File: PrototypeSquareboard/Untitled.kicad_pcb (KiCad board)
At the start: 2 copper layers, 131.9 x 97.8 mm, 35 parts

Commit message: square and flower boards at V4
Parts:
- added G***: LOGO, Symbol:UCR_logo_1.4cm, F.Cu at (71.8, 87.0)
- added G***: LOGO, Symbol:Consortium_logo_1pt4cm, F.Cu at (71.6, 99.0)
- G*** (x2): moved to B.Cu
- REF** (x4): footprint SiPM:S14160-3015PS_copy -> SiPM:S14160-3015PS_copy2
- moved G*** 70.4 mm to (89.0, 40.0), turned to 180 degrees
- moved G*** 35.8 mm to (86.6, 74.4), turned to 180 degrees
- moved G*** 8.11 mm to (138.7, 82.2)
- moved REF** 2.20 mm to (66.0, 36.6)
- moved REF** 2.10 mm to (66.0, 47.7)
- moved REF** 1.20 mm to (66.0, 59.2)
- moved REF** 1.00 mm to (66.0, 70.6)
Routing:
- net (no net): track 2555.4 -> 2562.2 mm
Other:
- board text added: "1 2 3 4"
- board text added: "Designed by Sebouh J Paul Version 4"
- board text removed: "1"
- board text removed: "2"
- board text removed: "3"
- board text removed: "4"
- board text removed: "Designed by Sebouh J Paul Version 3"

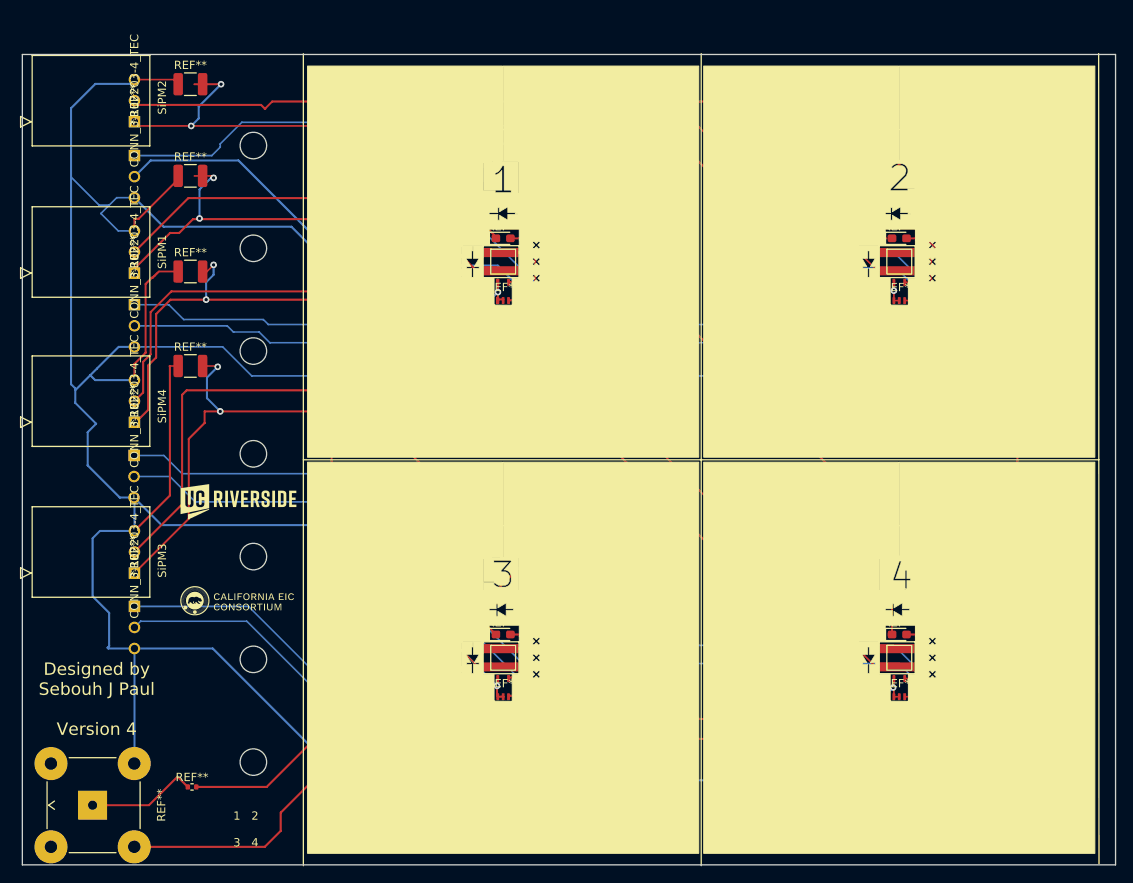
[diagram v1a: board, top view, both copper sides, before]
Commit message: v5 of the prototype hexboard and squareboards:  added label to capacitors and resistors; moved temperature sensors to periphery; added 0.1 mm back to top and bottom of boards
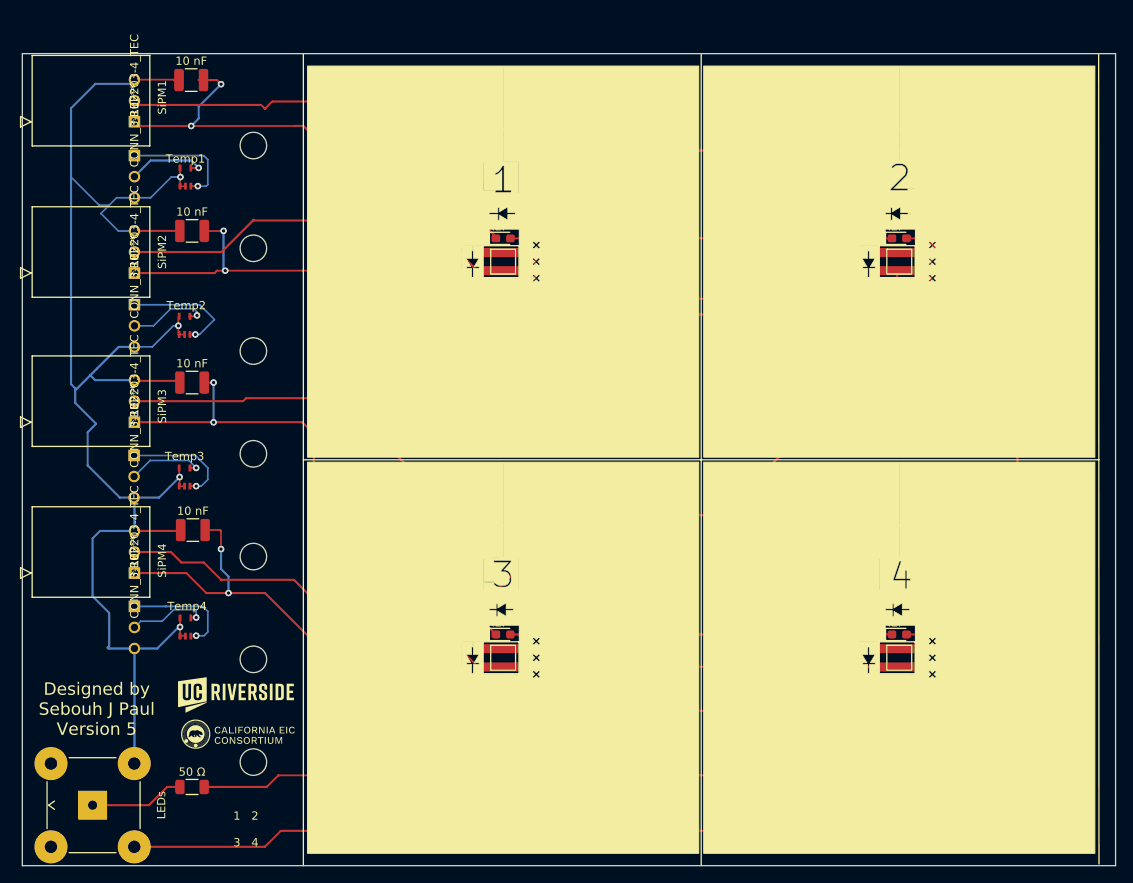
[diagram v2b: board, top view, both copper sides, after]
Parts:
- removed ? (x2): , 
- 10 nF: renamed from REF** (x4)
- 50 Ω: renamed from REF**; value R_0402_1005Metric -> R_1206_3216Metric; footprint Resistor_SMD:R_0402_1005Metric -> Resistor_SMD:R_1206_3216Metric
- moved Temp4 86.4 mm to (65.4, 102.1)
- moved Temp2 86.3 mm to (65.3, 65.7)
- moved Temp3 46.1 mm to (65.3, 84.0)
- moved Temp1 40.7 mm to (65.4, 47.8)
- moved G*** 23.3 mm to (71.5, 110.3)
- moved 10 nF 19.8 mm to (66.3, 90.4)
- moved G*** 16.1 mm to (71.7, 115.1)
- moved 10 nF 13.4 mm to (66.2, 72.6)
- moved 10 nF 6.64 mm to (66.2, 54.3)
- moved G*** 6.61 mm to (90.9, 79.4)
- moved G*** 1.08 mm to (90.0, 39.6)
- moved 10 nF 0.51 mm to (66.1, 36.1)
- renumbered REF** to LEDs, REF** to Temp1, REF** to Temp2, REF** to Temp3, REF** to Temp4
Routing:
- net (no net): track 2562.2 -> 1613.3 mm
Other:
- board size 131.9 x 97.8 mm -> 131.9 x 98 mm
- board text added: "Designed by Sebouh J Paul Version 5"
- board text removed: "Designed by Sebouh J Paul Version 4"

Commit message: v6 of square and hex boards: traces in back in the area where the scints are to be placed.
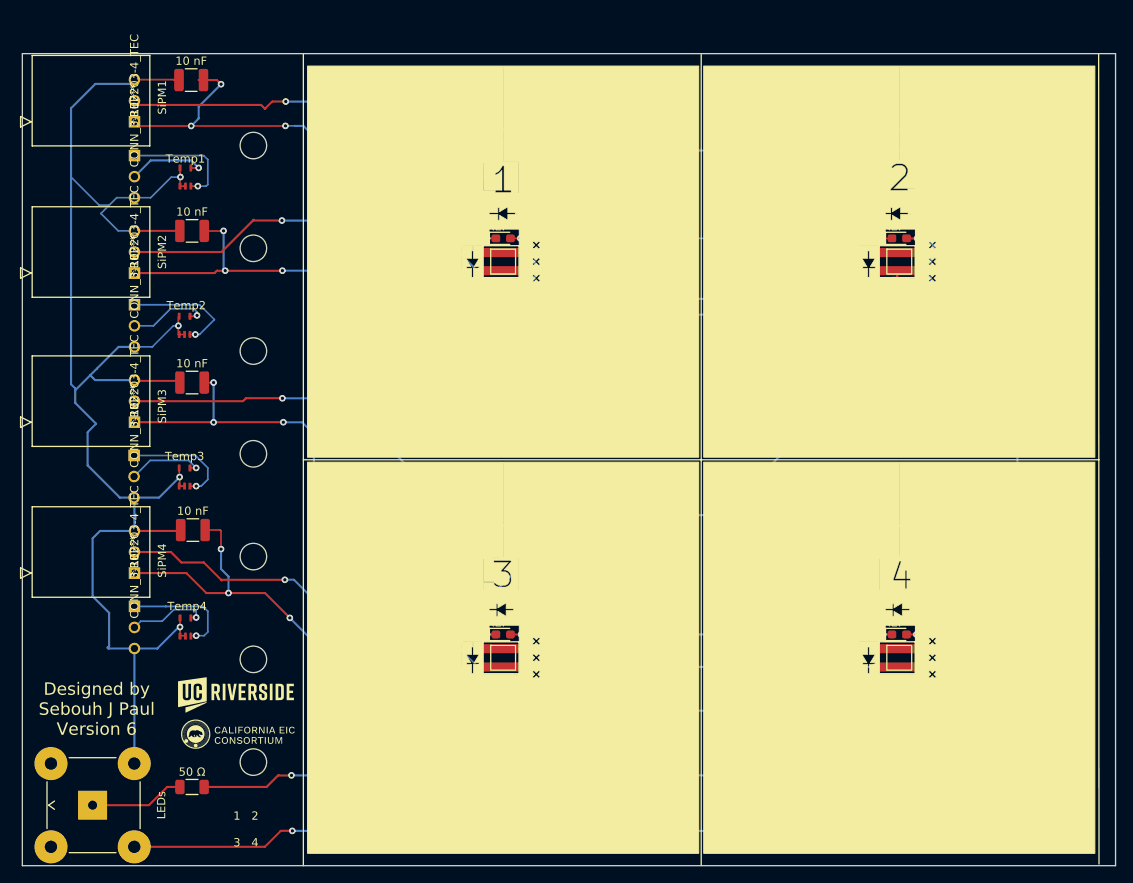
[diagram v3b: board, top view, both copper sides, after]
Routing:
- net (no net): track 1613.3 -> 1612.2 mm, vias 20 -> 46
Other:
- board text added: "Designed by Sebouh J Paul Version 6"
- board text removed: "Designed by Sebouh J Paul Version 5"

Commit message: removed extraneous traces on front of square-cell board
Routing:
- net (no net): track 1612.2 -> 1604.7 mm
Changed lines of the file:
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@@
   (segment (start 63.9725 36.0475) (end 64.525 36.6) (width 0.2) (layer "F.Cu") (net 0))
   (segment (start 54.2 123.6) (end 61 123.6) (width 0.25) (layer "F.Cu") (net 0))
-  (segment (start 106.2 64.4) (end 107 64.4) (width 0.25) (layer "F.Cu") (net 0))
   (segment (start 64.7 85.05) (end 64.65 85.1) (width 0.2) (layer "F.Cu") (net 0))
   (segment (start 69.7 92.7) (end 69.7 90.5) (width 0.2) (layer "F.Cu") (net 0))
@@
   (segment (start 64.55 66.8) (end 65.2 66.8) (width 0.2) (layer "F.Cu") (net 0))
   (segment (start 63.525 90.5075) (end 64.7175 90.5075) (width 0.25) (layer "F.Cu") (net 0))
-  (segment (start 94.45 52.95) (end 96.9 55.4) (width 0.25) (layer "F.Cu") (net 0))
   (segment (start 59.2501 56.8475) (end 69.7525 56.8475) (width 0.25) (layer "F.Cu") (net 0))
   (segment (start 67.613497 94.313497) (end 69.7 96.4) (width 0.25) (layer "F.Cu") (net 0))
@@
   (segment (start 104.615 55.2) (end 105.8 55.2) (width 0.2) (layer "F.Cu") (net 0))
   (segment (start 59.2501 93.0475) (end 63.6475 93.0475) (width 0.25) (layer "F.Cu") (net 0))
-  (segment (start 132.3 86.3) (end 130 88.6) (width 0.25) (layer "F.Cu") (net 0))
   (segment (start 102.865 55.2) (end 101.8 55.2) (width 0.2) (layer "F.Cu") (net 0))
   (segment (start 152.215 55.2) (end 153.7 55.2) (width 0.25) (layer "F.Cu") (net 0))

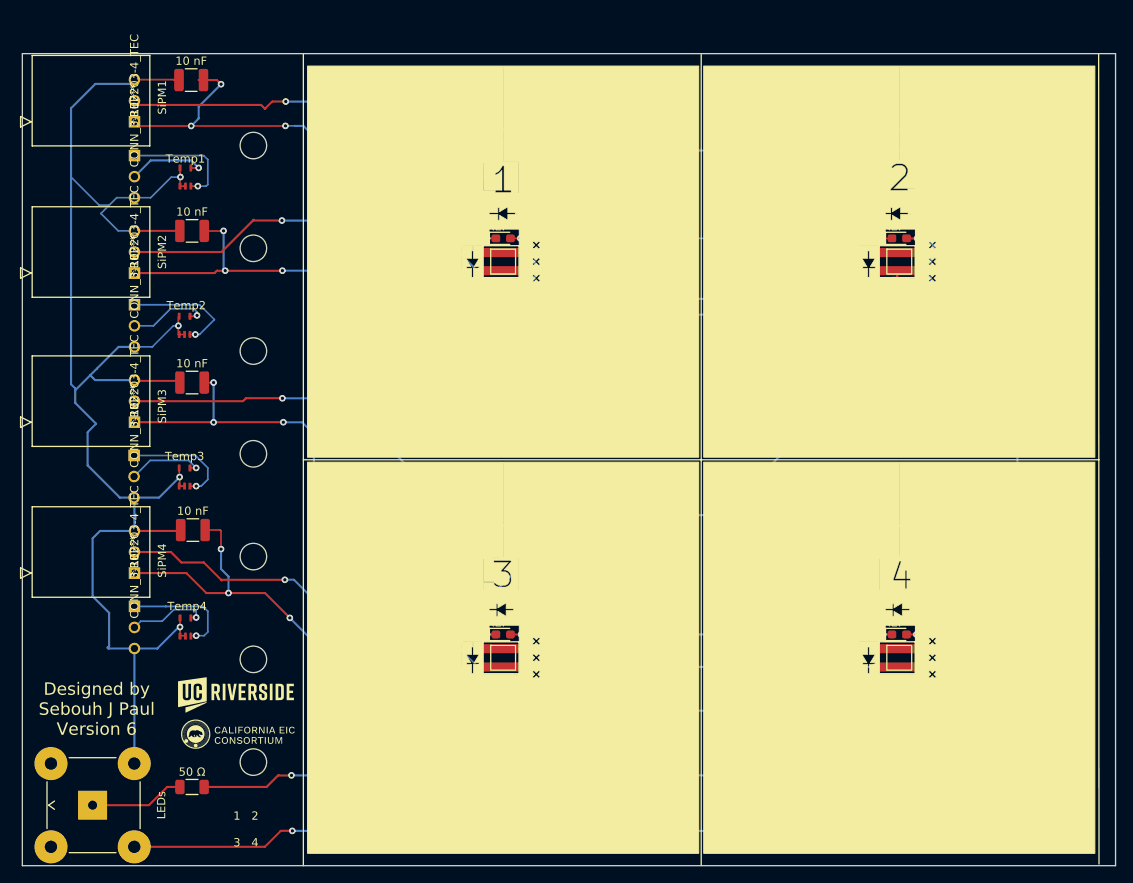
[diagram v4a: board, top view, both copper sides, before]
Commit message: v7 square board.  1.3 mm SiPMs, vias inside dimples, and excessive silkscreen removed outside dimple
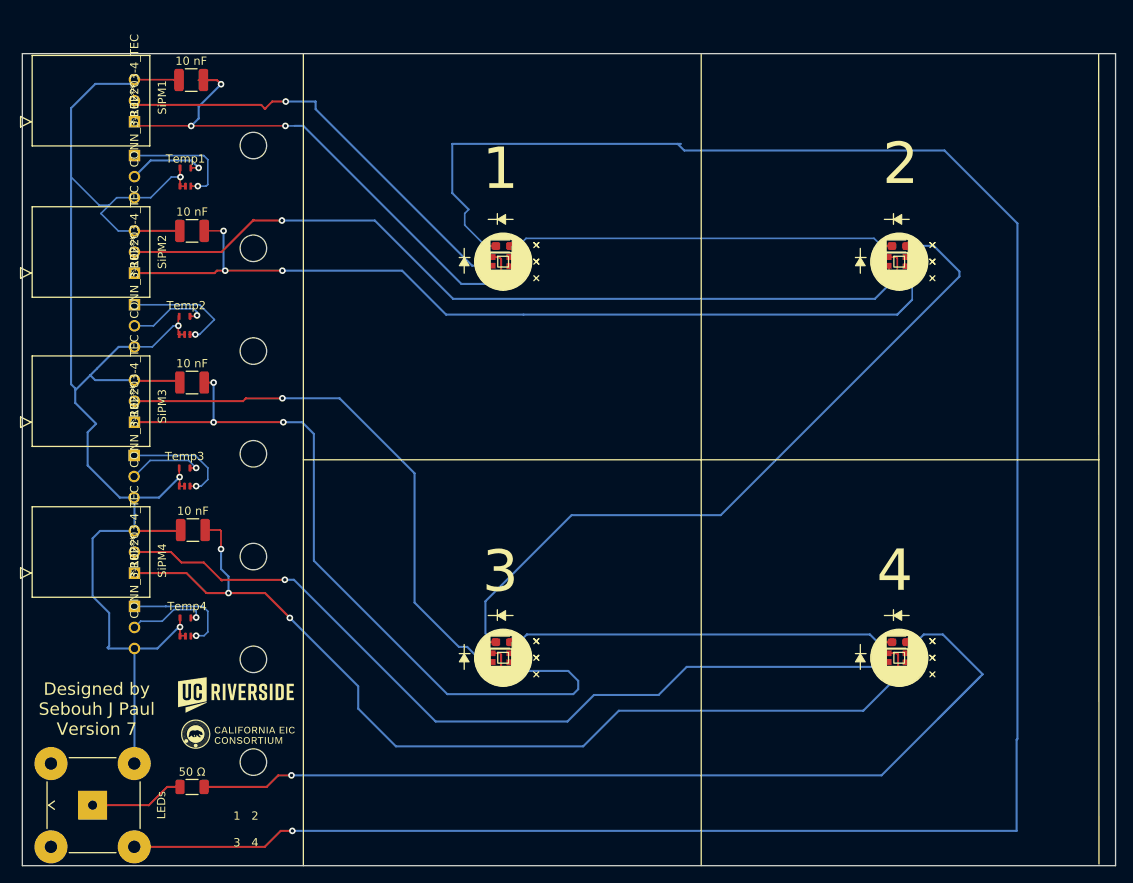
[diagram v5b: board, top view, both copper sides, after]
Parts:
- removed the REF** at (103.8, 52.2)
- removed the REF** at (151.5, 55.2)
- removed the REF** at (151.2, 52.2)
- removed the REF** at (103.7, 55.2)
- removed the REF** at (151.5, 103.0)
- removed the REF** at (151.4, 100.0)
- removed the REF** at (103.6, 100.0)
- removed the REF** at (103.7, 103.0)
- REF** (x4): footprint SiPM:S14160-3015PS_copy2 -> SiPM:S14160-1315PS_dimple_silkscreen_with_LED_copy
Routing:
- net (no net): track 1604.7 -> 1582.7 mm
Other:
- board text added: "1"
- board text added: "2"
- board text added: "3"
- board text added: "4"
- board text added: "Designed by Sebouh J Paul Version 7"
- board text removed: "Designed by Sebouh J Paul Version 6"
